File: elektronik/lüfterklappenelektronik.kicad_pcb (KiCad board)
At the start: 4 copper layers, 80 x 87.6 mm, 115 parts, among them J101 Conn_01x05_Male, J102 Ckmtw_2510S-2P, J103 Conn_LAN_ENC28J60, J104 USB_B_Micro, J106 WJ2EDGVC-5.08-2P, J107 WJ2EDGVC-5.08-2P, J108 WJ2EDGVC-5.08-2P, P101 PWR_BUS_CONN, P103 PressureSensor3, P104 PressureSensor1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

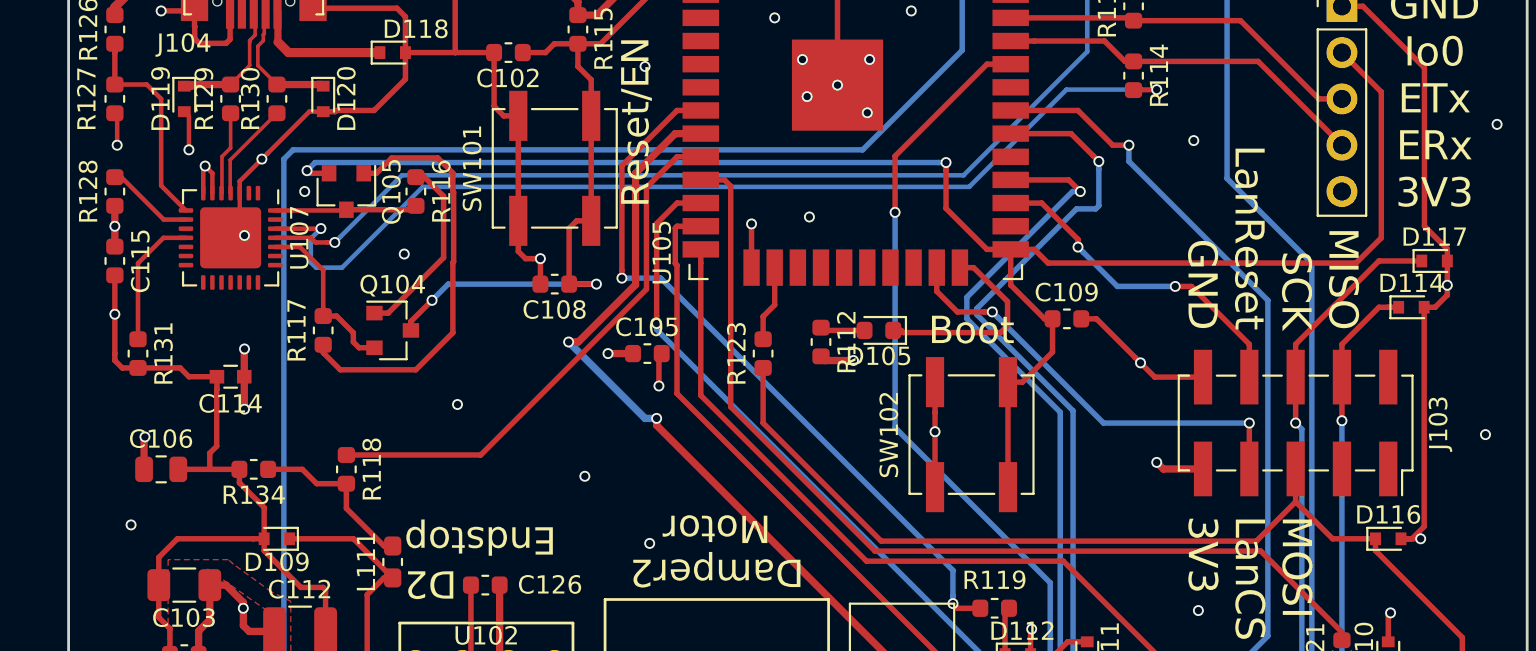
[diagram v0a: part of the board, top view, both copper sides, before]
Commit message: usb d- d+ bugfix
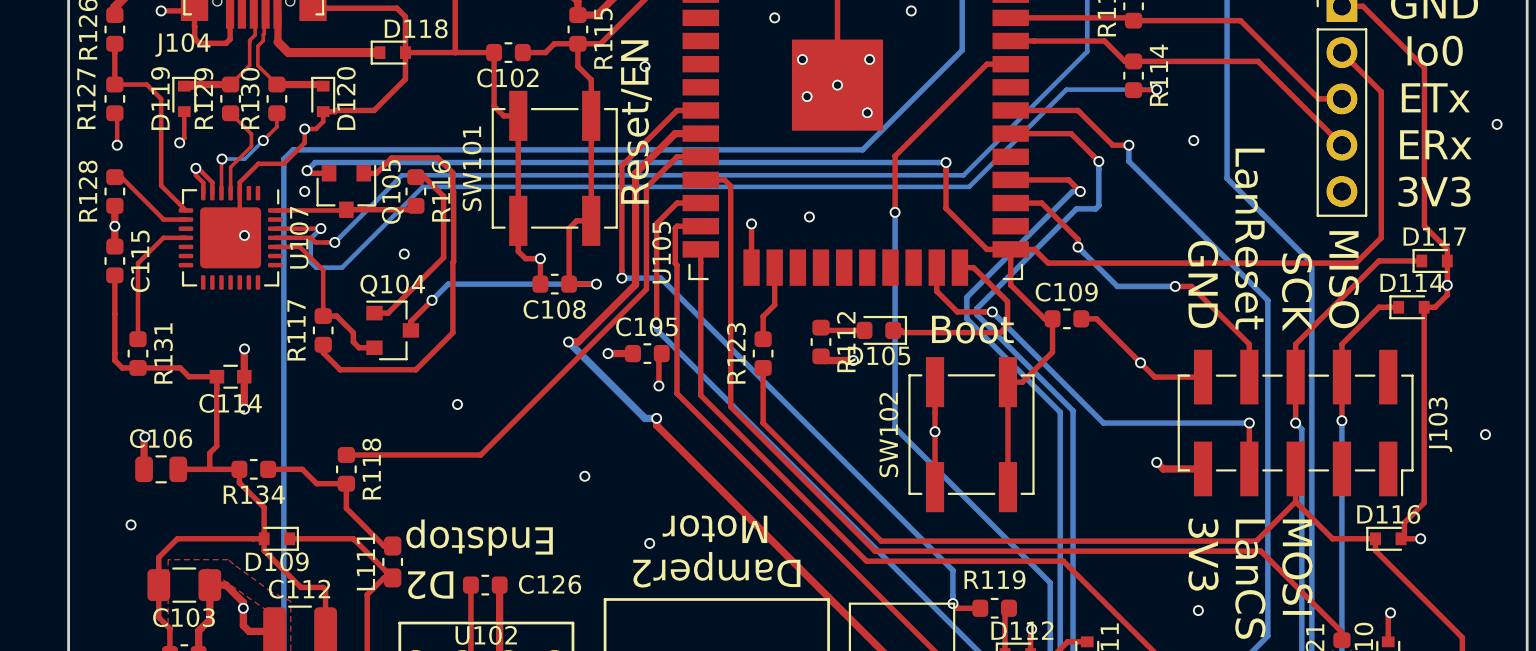
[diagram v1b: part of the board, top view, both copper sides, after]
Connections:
- D119 pad 1: /UCD- -> /UCD+
- D120 pad 1: /UCD+ -> /UCD-
- J104 pad 2: /UCD+ -> /UCD-
- J104 pad 3: /UCD- -> /UCD+
- R129 pad 1: /USB_D- -> /USB_D+
- R129 pad 2: /UCD- -> /UCD+
- R130 pad 1: /USB_D+ -> /USB_D-
- R130 pad 2: /UCD+ -> /UCD-
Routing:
- net GND: track 627.2 -> 636.7 mm, vias 55 -> 54
- net +3V3: track 304.2 -> 313.3 mm
- net /USB_D-: track 4.59 -> 6.37 mm, vias 0 -> 2
